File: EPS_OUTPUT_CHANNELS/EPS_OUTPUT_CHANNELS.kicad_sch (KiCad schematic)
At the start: 65 parts, among them J5901 VBUS, J5902 Chan, J5903 Chan, J5904 Chan, J5905 Chan

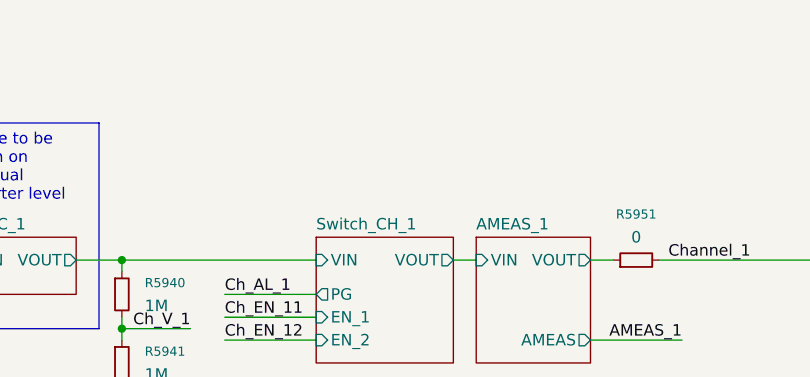
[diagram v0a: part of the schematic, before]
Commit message: added universal switch, added simples current source, reworked test schematic and pcb
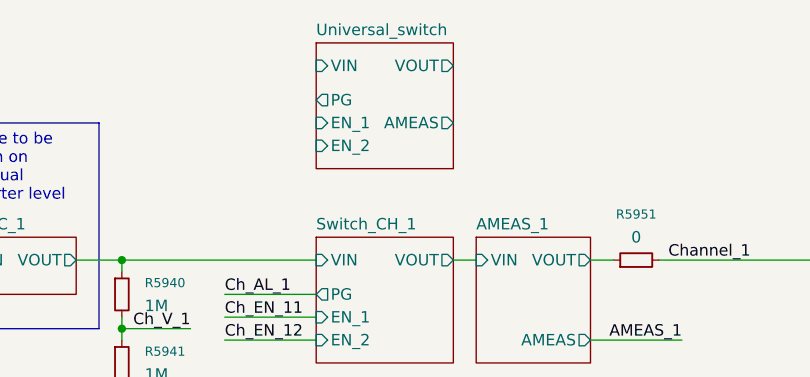
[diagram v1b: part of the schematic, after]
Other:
- added sheet Universal_switch (../UniversalSwitch.kicad_sch)
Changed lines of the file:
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@@
+	)
+	(sheet
+		(at 156.21 16.51)
+		(size 15.24 13.97)
+		(exclude_from_sim no)
+		(in_bom yes)
+		(on_board yes)
+		(dnp no)
+		(fields_autoplaced yes)
+		(stroke
+			(width 0.1524)
+			(type solid)
+		)
+		(fill
+			(color 0 0 0 0.0000)
+		)
+		(property "Sheetname" "Universal_switch"
+			(at 156.21 15.7984 0)
+			(effects
+				(font
+					(size 1.27 1.27)
+				)
+				(justify left bottom)
+			)
+		)
+		(property "Sheetfile" "../UniversalSwitch.kicad_sch"
+			(at 156.21 31.0646 0)
+			(effects
+				(font
+					(size 1.27 1.27)
+				)
+				(justify left top)
+				(hide yes)
+			)
+		)
+		(pin "AMEAS" output
+			(at 171.45 25.4 0)
+			(effects
+				(font
+					(size 1.27 1.27)
+				)
+				(justify right)
+			)
+		)
+		(pin "EN_1" input
+			(at 156.21 25.4 180)
+			(effects
+				(font
+					(size 1.27 1.27)
+				)
+				(justify left)
+			)
+		)
+		(pin "EN_2" input
+			(at 156.21 27.94 180)
+			(effects
+				(font
+					(size 1.27 1.27)
+				)
+				(justify left)
+			)
+		)
+		(pin "PG" output
+			(at 156.21 22.86 180)
+			(effects
+				(font
+					(size 1.27 1.27)
+				)
+				(justify left)
+			)
+		)
+		(pin "VIN" input
+			(at 156.21 19.05 180)
+			(effects
+				(font
+					(size 1.27 1.27)
+				)
+				(justify left)
+			)
+		)
+		(pin "VOUT" output
+			(at 171.45 19.05 0)
+			(effects
+				(font
+					(size 1.27 1.27)
+				)
+				(justify right)
+			)
+		)
+		(instances
+			(project "EPS"
+				(path "/94201994-47b8-4213-8d1a-05da12b2a7b0/2939b268-15b7-411b-af55-ccc6daa126bc"
+					(page "68")
+				)
+			)
+		)
 	)
 	(sheet

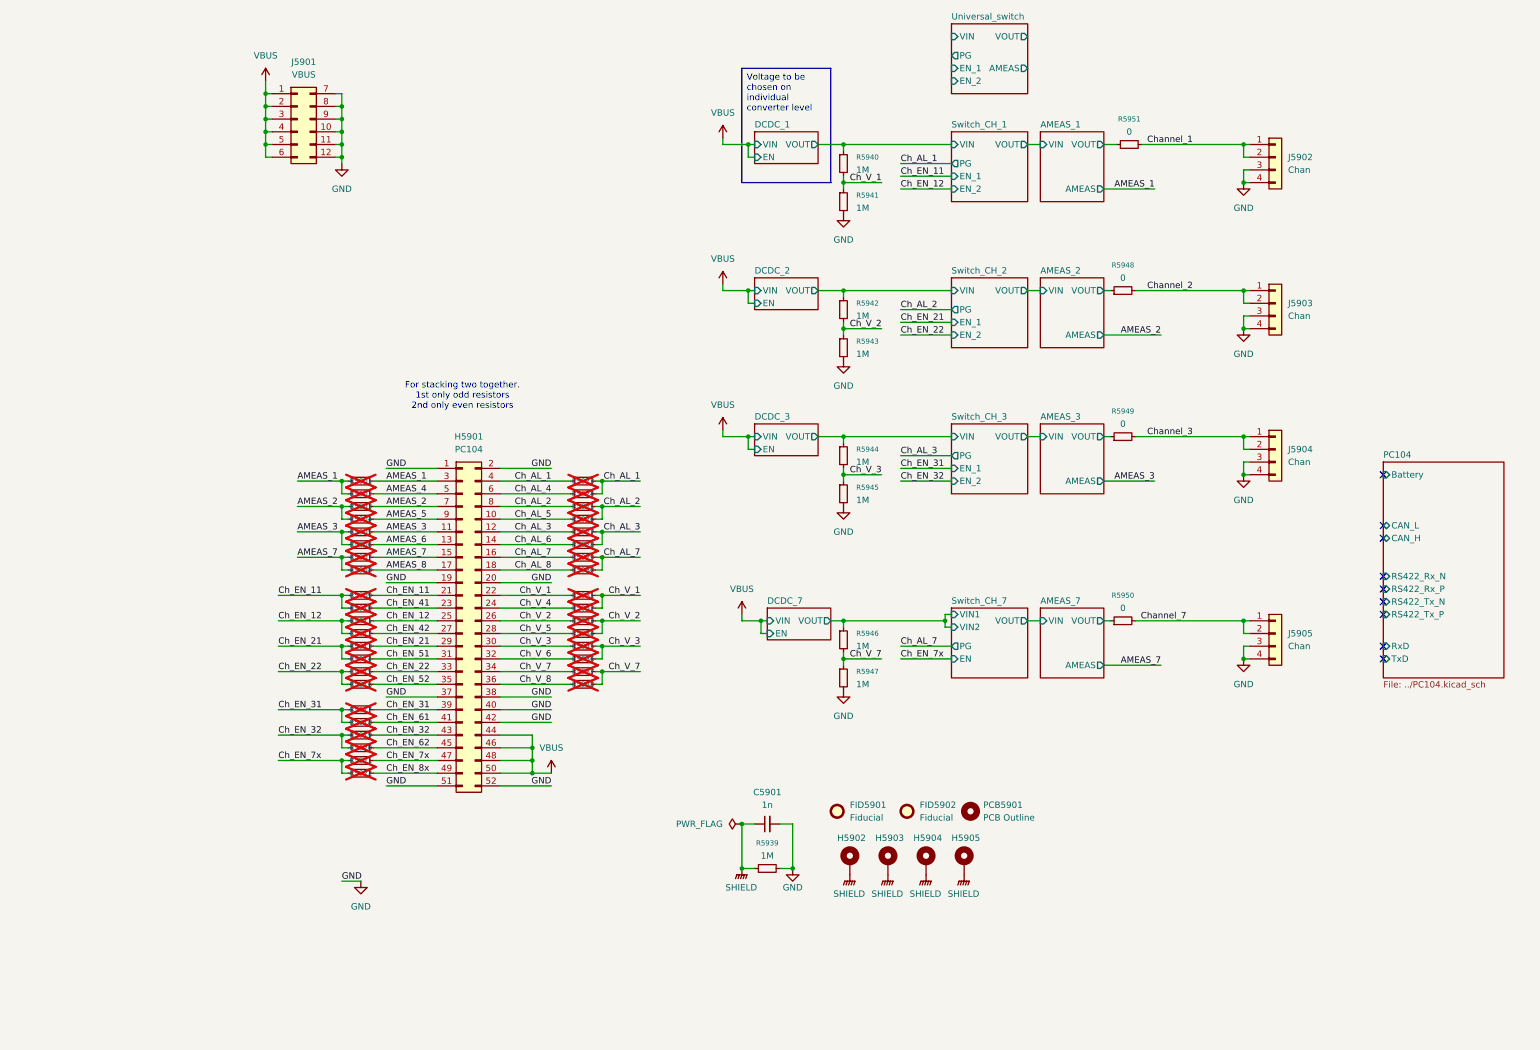
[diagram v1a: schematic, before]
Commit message: pcb progres for all components
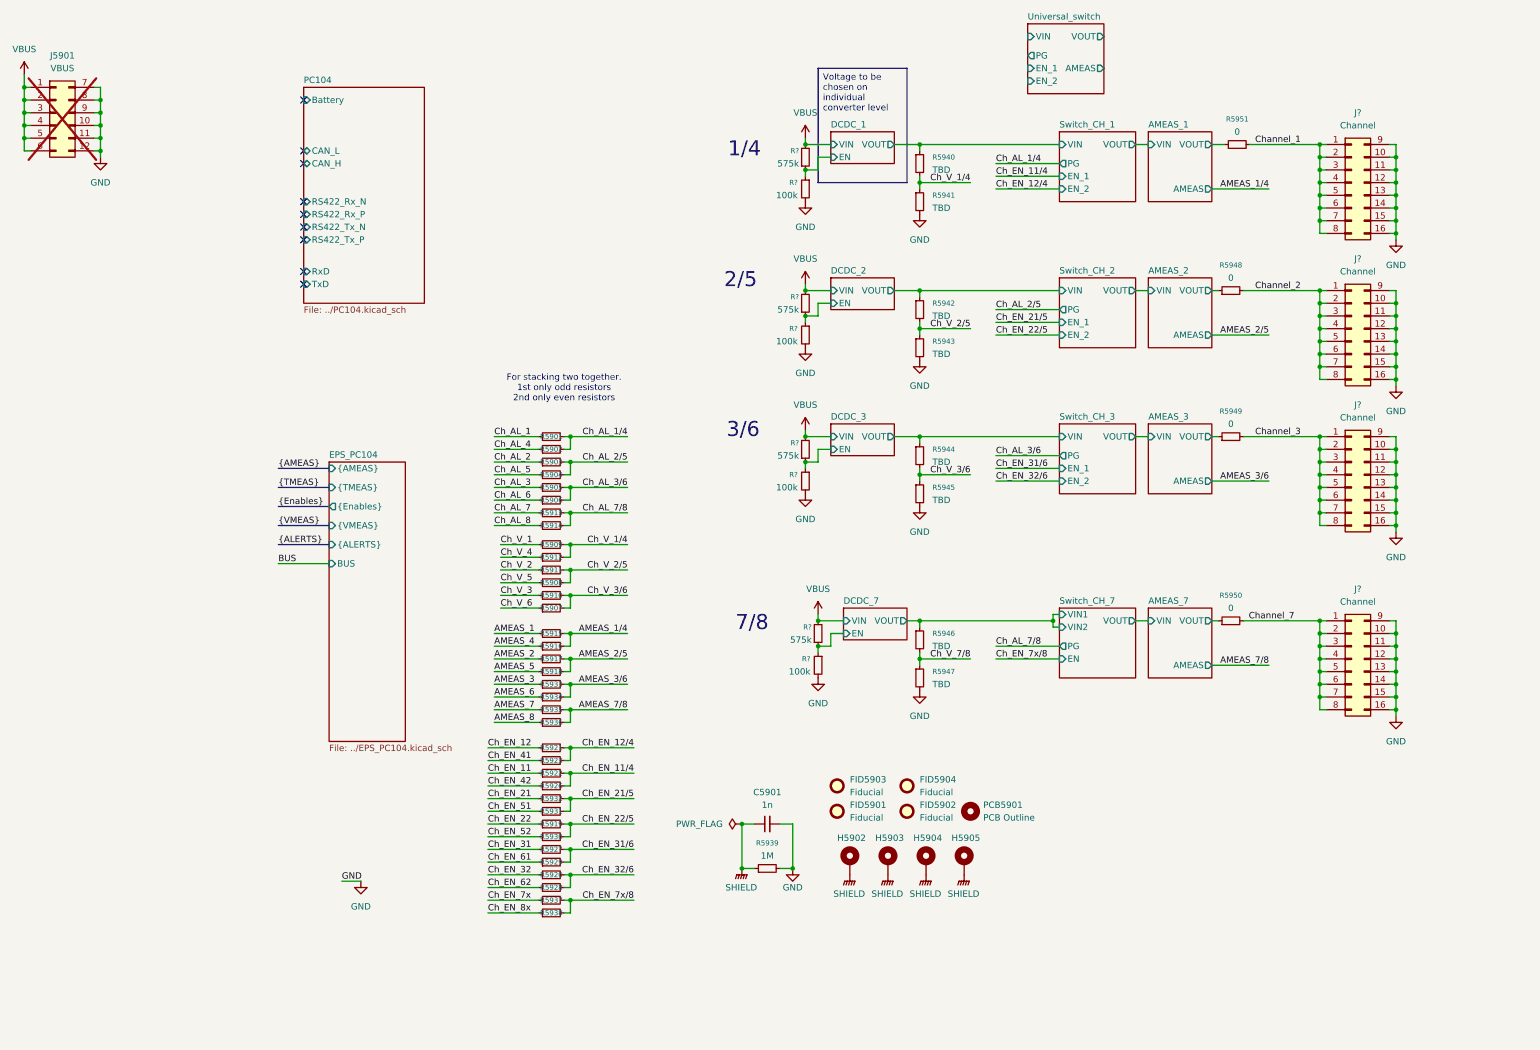
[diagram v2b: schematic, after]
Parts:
- removed H5901: PC104, Connector_PinSocket_2.54mm:PinSocket_2x26_P2.54mm_Vertical, symbol Connector_Generic:Conn_02x26_Odd_Even
- removed J5902, J5903, J5904, J5905: Chan, Connector_Molex:Molex_CLIK-Mate_502494-0470_1x04-1MP_P2.00mm_Horizontal, symbol Connector_Generic:Conn_01x04
- removed R5924, R5925: 0, Resistor_SMD:R_0603_1608Metric_Pad0.98x0.95mm_HandSolder, symbol Device:R_Small
- added FID5903, FID5904: Fiducial, Fiducial:Fiducial_1mm_Mask2mm, symbol Mechanical:Fiducial
- added J? (x4): Channel, Outlines:G125-MH11605L1P, symbol Connector_Generic:Conn_02x08_Top_Bottom
- added R? (x4): 575k, Resistor_SMD:R_0603_1608Metric_Pad0.98x0.95mm_HandSolder, symbol Device:R_Small
- added R? (x4): 100k, Resistor_SMD:R_0603_1608Metric_Pad0.98x0.95mm_HandSolder, symbol Device:R_Small
- J5901: now not fitted; now left out of the parts list
- R5901, R5902, R5903, R5904, R5905, R5906, R5907, R5908, R5909, R5910, R5911, R5912, R5913, R5914, R5915, R5916, R5917, R5918, R5919, R5920, R5921, R5922, R5923, R5926, R5927, R5928, R5929, R5930, R5931, R5932, R5933, R5934, R5935, R5936, R5937, R5938: now fitted
- R5940, R5941, R5942, R5943, R5944, R5945, R5946, R5947: value 1M -> TBD
- R5948, R5949, R5950, R5951: footprint Resistor_SMD:R_0603_1608Metric_Pad0.98x0.95mm_HandSolder -> Resistor_SMD:R_1210_3225Metric_Pad1.30x2.65mm_HandSolder
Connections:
- net Ch_V_8 is gone; now on net Ch_EN_8x: R5938.1
- net AMEAS_1: now also R5915.1; no longer R5901.1, R5901.2, R5902.1
- net AMEAS_2: now also R5917.1; no longer R5903.1, R5903.2, R5904.1
- net AMEAS_3: now also R5933.1; no longer R5905.1, R5905.2, R5906.1
- net AMEAS_4: now also R5916.1; no longer R5902.2
- net AMEAS_5: now also R5918.1; no longer R5904.2
- net AMEAS_6: now also R5934.1; no longer R5906.2
- net AMEAS_7: now also R5935.1; no longer R5907.1, R5907.2, R5908.1
- net AMEAS_8: now also R5936.1; no longer R5908.2
- net Ch_AL_1: now also R5901.1; no longer R5923.1, R5923.2
- net Ch_AL_2: now also R5903.1; no longer R5926.2
- net Ch_AL_3: now also R5905.1; no longer R5927.1, R5927.2, R5928.2
- net Ch_AL_4: now also R5902.1
- net Ch_AL_5: now also R5904.1; no longer R5926.1
- net Ch_AL_6: now also R5906.1; no longer R5928.1
- net Ch_AL_7: now also R5913.1; no longer R5929.1, R5929.2, R5930.2
- net Ch_AL_8: now also R5914.1; no longer R5930.1
- net Ch_EN_11: now also R5922.1; no longer R5909.1, R5909.2, R5910.1
- net Ch_EN_12: now also R5921.1; no longer R5911.1, R5911.2, R5912.1
- net Ch_EN_21: now also R5932.1; no longer R5913.1, R5913.2, R5914.1
- net Ch_EN_22: now also R5919.1; no longer R5915.1, R5915.2, R5916.1
- net Ch_EN_31: now also R5927.1; no longer R5917.1, R5917.2, R5918.1
- net Ch_EN_32: no longer R5919.1, R5919.2
- net Ch_EN_41: now also R5923.1; no longer R5910.2
- net Ch_EN_42: now also R5926.1; no longer R5912.2
- net Ch_EN_51: now also R5931.1; no longer R5914.2
- net Ch_EN_52: now also R5930.1; no longer R5916.2
- net Ch_EN_61: now also R5929.1; no longer R5918.2
- net Ch_EN_62: now also R5928.1; no longer R5920.2
- net Ch_EN_7x: now also R5937.1; no longer R5921.1, R5921.2, R5922.1
- net Ch_EN_8x: no longer R5922.2
- net Ch_V_1: now also R5909.1; no longer R5931.1, R5931.2, R5932.2, R5940.2, R5941.1
- net Ch_V_2: now also R5911.1; no longer R5933.1, R5933.2, R5934.2, R5942.2, R5943.1
- net Ch_V_3: now also R5910.1; no longer R5935.1, R5935.2, R5936.2, R5944.2, R5945.1
- net Ch_V_4: now also R5912.1; no longer R5932.1
- net Ch_V_5: now also R5908.1; no longer R5934.1
- net Ch_V_6: now also R5907.1; no longer R5936.1
- net Channel_1: now also J?.1 (Pin_1), J?.2 (Pin_2), J?.3 (Pin_3), J?.4 (Pin_4), J?.5 (Pin_5), J?.6 (Pin_6), J?.7 (Pin_7), J?.8 (Pin_8)
- net Channel_2: now also J?.1 (Pin_1), J?.2 (Pin_2), J?.3 (Pin_3), J?.4 (Pin_4), J?.5 (Pin_5), J?.6 (Pin_6), J?.7 (Pin_7), J?.8 (Pin_8)
- net Channel_3: now also J?.1 (Pin_1), J?.2 (Pin_2), J?.3 (Pin_3), J?.4 (Pin_4), J?.5 (Pin_5), J?.6 (Pin_6), J?.7 (Pin_7), J?.8 (Pin_8)
- net Channel_7: now also J?.1 (Pin_1), J?.2 (Pin_2), J?.3 (Pin_3), J?.4 (Pin_4), J?.5 (Pin_5), J?.6 (Pin_6), J?.7 (Pin_7), J?.8 (Pin_8)
- net GND: now also J?.10 (Pin_10), J?.10 (Pin_10), J?.10 (Pin_10), J?.10 (Pin_10), J?.11 (Pin_11), J?.11 (Pin_11), J?.11 (Pin_11), J?.11 (Pin_11), J?.12 (Pin_12), J?.12 (Pin_12), J?.12 (Pin_12), J?.12 (Pin_12), J?.13 (Pin_13), J?.13 (Pin_13), J?.13 (Pin_13), J?.13 (Pin_13), J?.14 (Pin_14), J?.14 (Pin_14), J?.14 (Pin_14), J?.14 (Pin_14), J?.15 (Pin_15), J?.15 (Pin_15), J?.15 (Pin_15), J?.15 (Pin_15), J?.16 (Pin_16), J?.16 (Pin_16), J?.16 (Pin_16), J?.16 (Pin_16), J?.9 (Pin_9), J?.9 (Pin_9), J?.9 (Pin_9), J?.9 (Pin_9), R?.2, R?.2, R?.2, R?.2
- net VBUS: now also R?.2, R?.2, R?.2, R?.2
- removed net Ch_V_7: R5937.1, R5937.2, R5938.2, R5946.2, R5947.1
- new net AMEAS_1/4: R5915.2, R5916.2
- new net AMEAS_2/5: R5917.2, R5918.2
- new net AMEAS_3/6: R5933.2, R5934.2
- new net AMEAS_7/8: R5935.2, R5936.2
- new net Ch_AL_1/4: R5901.2, R5902.2
- new net Ch_AL_2/5: R5903.2, R5904.2
- new net Ch_AL_3/6: R5905.2, R5906.2
- new net Ch_AL_7/8: R5913.2, R5914.2
- new net Ch_EN_11/4: R5922.2, R5926.2
- new net Ch_EN_12/4: R5921.2, R5923.2
- new net Ch_EN_21/5: R5931.2, R5932.2
- new net Ch_EN_22/5: R5919.2, R5930.2
- new net Ch_EN_31/6: R5927.2, R5929.2
- new net Ch_EN_32/6: R5920.2, R5928.2
- new net Ch_EN_7x/8: R5937.2, R5938.2
- new net Ch_V_1/4: R5909.2, R5912.2, R5940.2, R5941.1
- new net Ch_V_2/5: R5908.2, R5911.2, R5942.2, R5943.1
- new net Ch_V_3/6: R5907.2, R5910.2, R5944.2, R5945.1
- new net Ch_V_7/8: R5946.2, R5947.1
- new net DCDC_1/EN: R?.1, R?.1
- new net DCDC_2/EN: R?.1, R?.1
- new net DCDC_3/EN: R?.1, R?.1
- new net DCDC_7/EN: R?.1, R?.1
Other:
- added sheet EPS_PC104 (../EPS_PC104.kicad_sch)
- note added: "1/4"
- note added: "2/5"
- note added: "3/6"
- note added: "7/8"
- moved on the sheet: R5940, R5941, R5942, R5943, R5944, R5945, R5946, R5947, R5948, R5949, R5950, R5951

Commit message: progress on PCBs
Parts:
- gave numbers to parts that had none: 12
- renumbered C5901 to C101, FID5903 to FID101, FID5904 to FID102, FID5901 to FID103, FID5902 to FID104, H5902 to H103, H5903 to H104, H5904 to H105, H5905 to H106, J5901 to J101, PCB5901 to PCB101, R5951 to R101, R5940 to R102, R5941 to R103, R5948 to R104, R5942 to R105, R5943 to R106, R5901 to R107, R5949 to R108, R5902 to R109, R5944 to R110, R5903 to R111, R5904 to R112, R5905 to R113, R5945 to R114, R5906 to R115, R5913 to R116, R5914 to R117, R5909 to R118, R5912 to R119, R5911 to R120, R5908 to R121, R5910 to R122, R5907 to R123, R5950 to R124, R5915 to R125, R5946 to R126, R5916 to R127, R5917 to R128, R5918 to R129, R5947 to R130, R5933 to R131, R5934 to R132, R5935 to R133, R5936 to R134, R5921 to R135, R5923 to R136, R5922 to R137, R5926 to R138, R5932 to R139, R5931 to R140, R5919 to R141, R5930 to R142, R5927 to R143, R5929 to R144, R5939 to R145, R5920 to R146, R5928 to R147, R5937 to R148, R5938 to R149
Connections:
- no-connect marks 9 -> 11
